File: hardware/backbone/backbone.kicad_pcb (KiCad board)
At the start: 4 copper layers, 31.3 x 68.9 mm, 113 parts, among them J1 RESET, J10 CORE_A, J11 MOUNT, J12 PW, J13 FIELD_B, J14 FIELD_A, J15 UART PROG, J16 ALED, J2 FROM_PREVIOUS, J4 FROM_PREVIOUS, J5 CONN_A, J6 BOOTLOADER, J7 CONN_B, J8 CORE_B, J9 TO NEXT, Q2 AO3401A, U11 470nH DCR=450m, U13 470nH DCR=450m, U15 ST25R100, U17 BLM18PG471SZ1D, U2 SN65HVD230DR, U4 AP2112K-3.3TRG1, U5 ESP32-C3-MINI-1-H4X, U8 G3VM-61VY3, U9 SN74AHCT1G14DCKR, X1 NX2016SA 27.12MHz

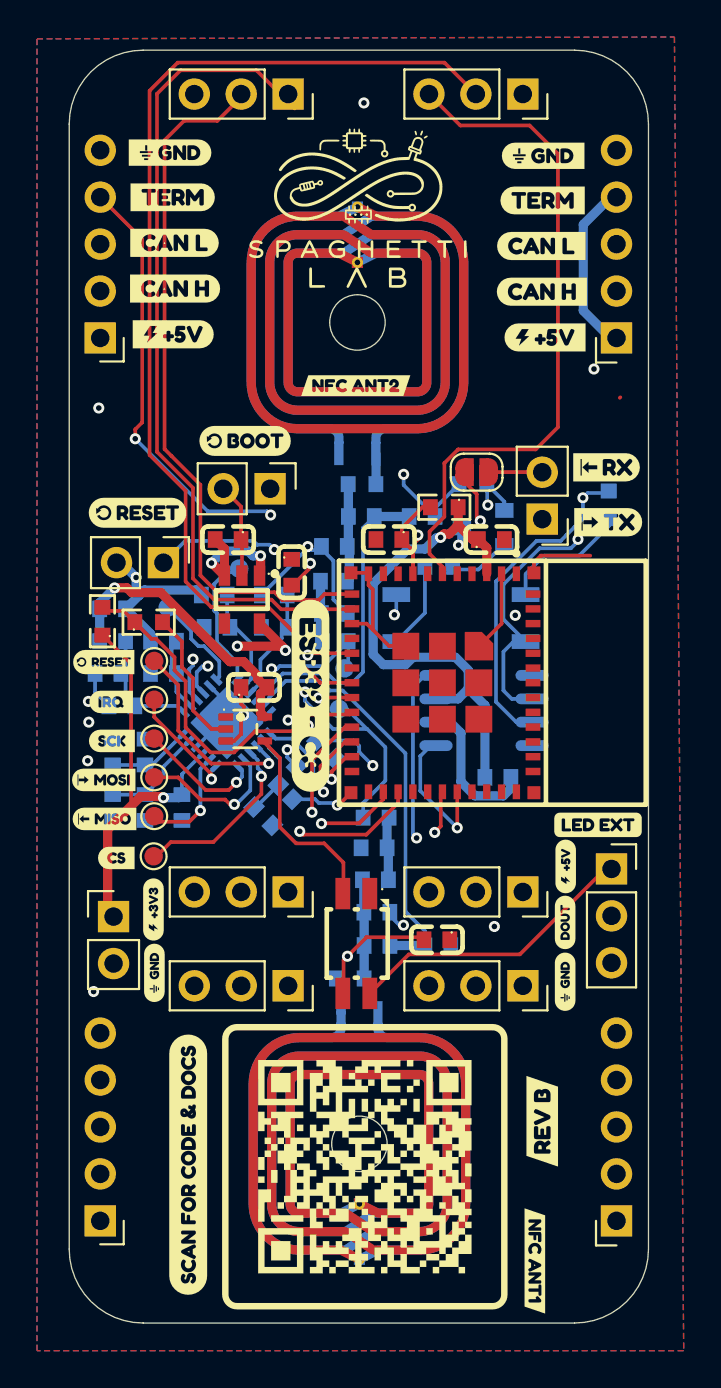
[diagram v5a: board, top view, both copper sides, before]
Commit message: Preserve Backbone USB hardware variant
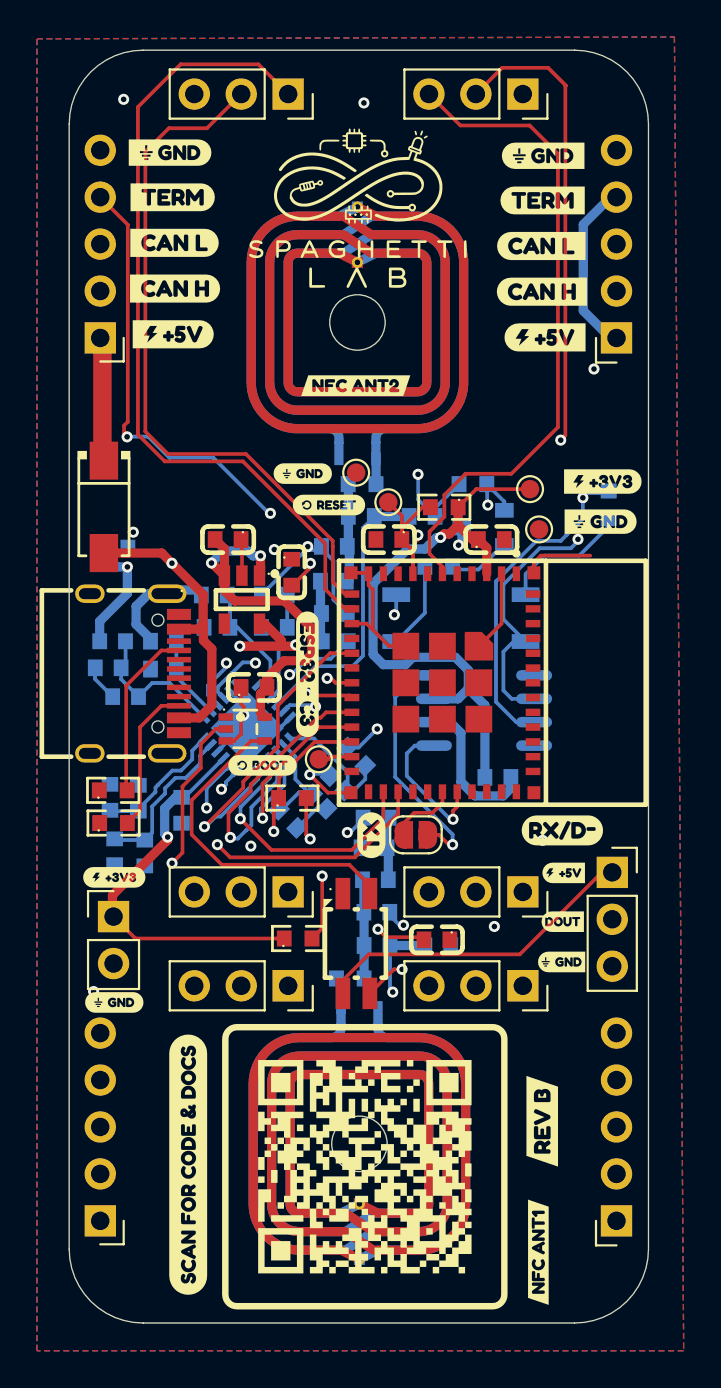
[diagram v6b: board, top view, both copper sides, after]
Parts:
- removed J1: RESET, Connector_PinHeader_2.54mm:PinHeader_1x02_P2.54mm_Vertical
- removed J15: UART PROG, Connector_PinHeader_2.54mm:PinHeader_1x02_P2.54mm_Vertical
- removed J6: BOOTLOADER, Connector_PinHeader_2.54mm:PinHeader_1x02_P2.54mm_Vertical
- removed TP10, TP11, TP14, TP16, TP6, TP7: SMD/0.6mm, TestPoint:TestPoint_Pad_D1.0mm
- removed TP17, TP2, TP20, TP4: SMD/0.8mm, TestPoint:TestPoint_Pad_D1.0mm
- removed kobee-studio-6AA83AC8, kobee-studio-6AA93B33, kobee-studio-6AA93B92, kobee-studio-6AA93C2C: Kobee Studio, kobee-studio-6AA82ECF
- removed kobee-studio-6AA83BE1: Kobee Studio, kobee-studio-6AA835EE
- removed kobee-studio-6AA93B26: Kobee Studio, kobee-studio-6AA82B88
- removed kobee-studio-6AA93B3B, kobee-studio-6AA93B41: Kobee Studio, kobee-studio-6AA82E83
- removed kobee-studio-6AA93B49: Kobee Studio, kobee-studio-6AA82EBC
- removed kobee-studio-6AA93B50: Kobee Studio, kobee-studio-6AA82E9A
- removed kobee-studio-6AA93B59: Kobee Studio, kobee-studio-6AA82E4A
- added D4: SS54_C22452, SpaghettiLAB:SMA_L4.4-W2.8-LS5.4-R-RD, F.Cu at (153.7, 87.4)
- added R20: 5.1k, SpaghettiLAB:R0603, F.Cu at (154.2, 104.5)
- added R23: 5.1k, SpaghettiLAB:R0603, F.Cu at (154.2, 102.7)
- added TP13: TestPoint, TestPoint:TestPoint_Pad_D1.0mm, F.Cu at (177.2, 88.6)
- added TP15: TestPoint, TestPoint:TestPoint_Pad_D1.0mm, F.Cu at (176.7, 86.4)
- added TP18: TestPoint, TestPoint:TestPoint_Pad_D1.0mm, F.Cu at (169.1, 87.1)
- added TP5: TestPoint, TestPoint:TestPoint_Pad_D1.0mm, F.Cu at (165.3, 101.0)
- added TP8: TestPoint, TestPoint:TestPoint_Pad_D1.0mm, F.Cu at (167.3, 85.5)
- added U1: HC-TYPE-C-16P-01A, SpaghettiLAB:USB-C-SMD_HC-TYPE-C-16P-01A, F.Cu at (155.3, 96.4)
- added kobee-studio-6AAA9A37: Kobee Studio, kobee-studio-6AA835EE, F.Cu at (165.9, 87.3)
- added kobee-studio-6AAA9A4A: Kobee Studio, kobee-studio-6AA835EE, F.Cu at (162.3, 101.3)
- added kobee-studio-6AAA9A97: Kobee Studio, kobee-studio-6AA82B88, F.Cu at (168.2, 105.1)
- added kobee-studio-6AAA9AEA: Kobee Studio, kobee-studio-6AA835EE, F.Cu at (180.7, 86.0)
- added kobee-studio-6AAA9AF2: Kobee Studio, kobee-studio-6AA835EE, F.Cu at (180.6, 88.2)
- added kobee-studio-6AAA9B66: Kobee Studio, kobee-studio-6AA83B2B, F.Cu at (178.4, 112.0)
- added kobee-studio-6AAA9B76: Kobee Studio, kobee-studio-6AA83B2B, F.Cu at (178.5, 109.8)
- C1, C12, C13, C16, C18, C20, C22, C23, C28, C3, C30, C32, C33, C35, C37, C39, C41, C43, C46, C48, C5, C51, C54, C55, C58, C60, C62, C63, C65, C7, C70, C72, C9: footprint SpaghettiLAB2:C0603 -> SpaghettiLAB:C0603
- LED1: footprint SpaghettiLAB2:LED-SMD_4P-L3.2-W2.8-LS5.9_SK6812MINI-E -> SpaghettiLAB:LED-SMD_4P-L3.2-W2.8-LS5.9_SK6812MINI-E
- R1, R11, R14, R2, R4, R5, R8, R9: footprint SpaghettiLAB2:R0603 -> SpaghettiLAB:R0603
- U2: footprint SpaghettiLAB:SOIC-8_L4.9-W3.9-P1.27-LS6.0-BL -> SpaghettiLAB:SOIC-8_L5.0-W4.0-P1.27-LS6.0-BL
- U4: footprint SpaghettiLAB2:SOT-25-5_L2.9-W1.6-P0.95-LS2.8-BL -> SpaghettiLAB:SOT-25-5_L2.9-W1.6-P0.95-LS2.8-BL
- U9: footprint SpaghettiLAB2:SOT-353_L2.2-W1.4-P0.65-LS2.4-BR -> SpaghettiLAB:SOT-353_L2.2-W1.4-P0.65-LS2.4-BR
- moved kobee-studio-6AA83B6C 30.9 mm to (164.4, 85.6), turned to 0 degrees
- moved R2 20.2 mm to (164.2, 110.7), turned to 0 degrees
- moved JP1 19.9 mm to (170.6, 105.1), turned to 0 degrees
- moved kobee-studio-6AAA9EE7 19.8 mm to (178.5, 104.9)
- moved R9 12.3 mm to (163.9, 103.1)
- moved C72 3.29 mm to (154.3, 89.6)
- moved kobee-studio-6AA83B72 2.74 mm to (154.2, 107.4), turned to 0 degrees
- moved kobee-studio-6AA83B6C 2.70 mm to (154.2, 114.2), turned to 0 degrees
- moved C35 2.53 mm to (155.5, 103.1)
- moved C30 2.46 mm to (155.9, 106.1)
- moved C39 2.45 mm to (154.0, 103.1)
- moved C33 2.40 mm to (154.3, 106.0)
- moved X1 1.90 mm to (165.8, 102.8)
- moved C18 1.67 mm to (167.3, 100.9)
- moved C20 1.35 mm to (163.6, 104.2)
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- renumbered kobee-studio-6AA834E9 to kobee-studio-6AAA99F5, kobee-studio-6AA83BBD to kobee-studio-6AAA9B47, kobee-studio-6AA93B20 to kobee-studio-6AAA9EE7
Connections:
- net Net-(J15-Pin_2) renamed /RX
- U15 pad 12: /TAD2_200 -> unconnected-(U15-TDA2-Pad12)
- U15 pad 13: /TAD1_200 -> unconnected-(U15-TAD1-Pad13)
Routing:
- net 5V: track 83.9 -> 220.4 mm, vias 5 -> 6
- net /RX: track 28.5 -> 3.78 mm, vias 1 -> 0
- net IO9/BOOT: track 23.4 -> 1.85 mm, vias 1 -> 0
- net CAN_TX: track 28.1 -> 8.02 mm
- net CAN_RX: track 31.9 -> 14.2 mm, vias 2 -> 1
- net VBUS: track 0.00 -> 16.0 mm, vias 0 -> 1
- net Net-(U9-A): track 7.53 -> 19.3 mm, vias 0 -> 2
- net /CC1: track 0.00 -> 9.33 mm
- net NFC_RST: track 20.6 -> 12.3 mm, vias 2 -> 1
- net /CC2: track 0.00 -> 8.05 mm
- net LED_DATA/STRAP: track 24.6 -> 17.0 mm
- net /TAD1_200: track 7.39 -> 0.00 mm
- net Net-(LED1-DIN): track 11.3 -> 18.4 mm
- net GND: track 76.5 -> 70.5 mm, vias 18 -> 14
- net /TAD2_200: track 5.63 -> 0.00 mm
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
